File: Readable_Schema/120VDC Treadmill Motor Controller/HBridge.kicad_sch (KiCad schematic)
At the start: 56 parts, among them J2 OSTT7020150, Q1 IPP60R060P7XKSA1, Q2 IPP60R060P7XKSA1, Q3 IPP60R060P7XKSA1, Q4 IPP60R060P7XKSA1, U1 UCC21530DWKR, U2 UCC21530DWKR

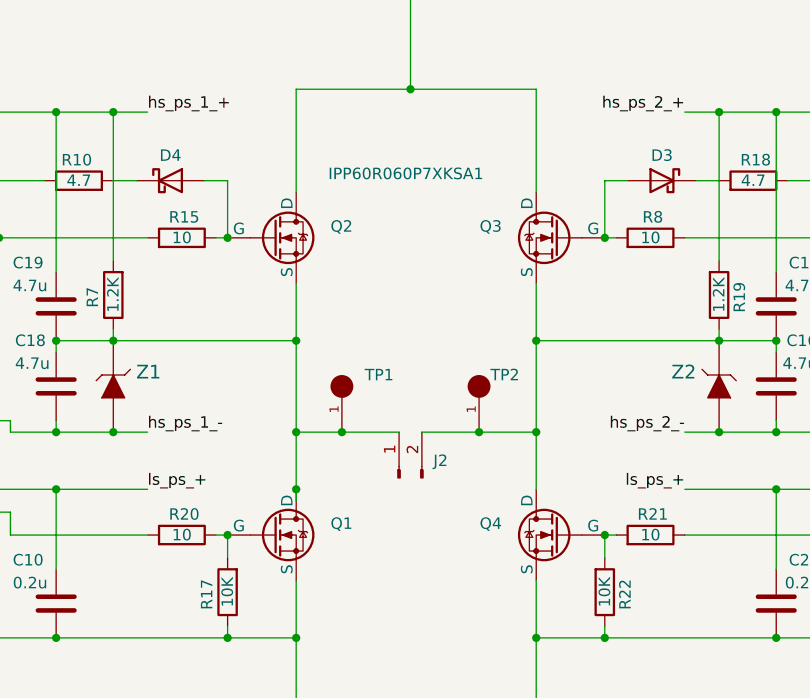
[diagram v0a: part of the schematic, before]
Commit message: -Updated kicad fet symbol to swap gate and drain numbers to match the datasheet
-There are not vertically mounted rectifier alternatives that are capable of 50 amps so stuck with the current one
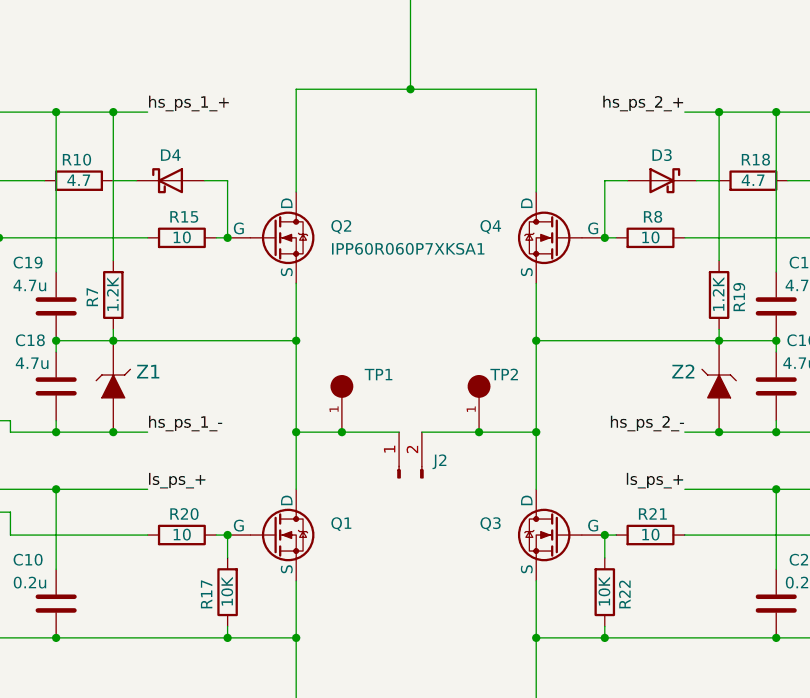
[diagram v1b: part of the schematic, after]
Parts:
- removed Q1, Q2, Q3, Q4: IPP60R060P7XKSA1, Package_TO_SOT_THT:TO-220-3_Vertical, symbol Simulation_SPICE:NMOS
- added Q1, Q2, Q3, Q4: IPP60R060P7XKSA1, Package_TO_SOT_THT:TO-220-3_Vertical, symbol Treadmill_Comp:IPP60R060P7XKSA1
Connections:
- net 170V Rect: now also Q2.2 (D), Q4.2 (D)
- net i_sense_+: now also Q1.3 (S), Q3.3 (S)
- net at D3.2 (A), R8.2: now also Q4.1 (G)
- net at C15.2, C16.1, J2.2 (Pin_2)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: now also Q3.2 (D), Q4.3 (S)
- net at C18.1, C19.2, J2.1 (Pin_1)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: now also Q1.2 (D), Q2.3 (S)
- net at D4.2 (A), R15.1: now also Q2.1 (G)
- net at R17.2, R20.1: now also Q1.1 (G)
- net at R21.2, R22.2: now also Q3.1 (G)

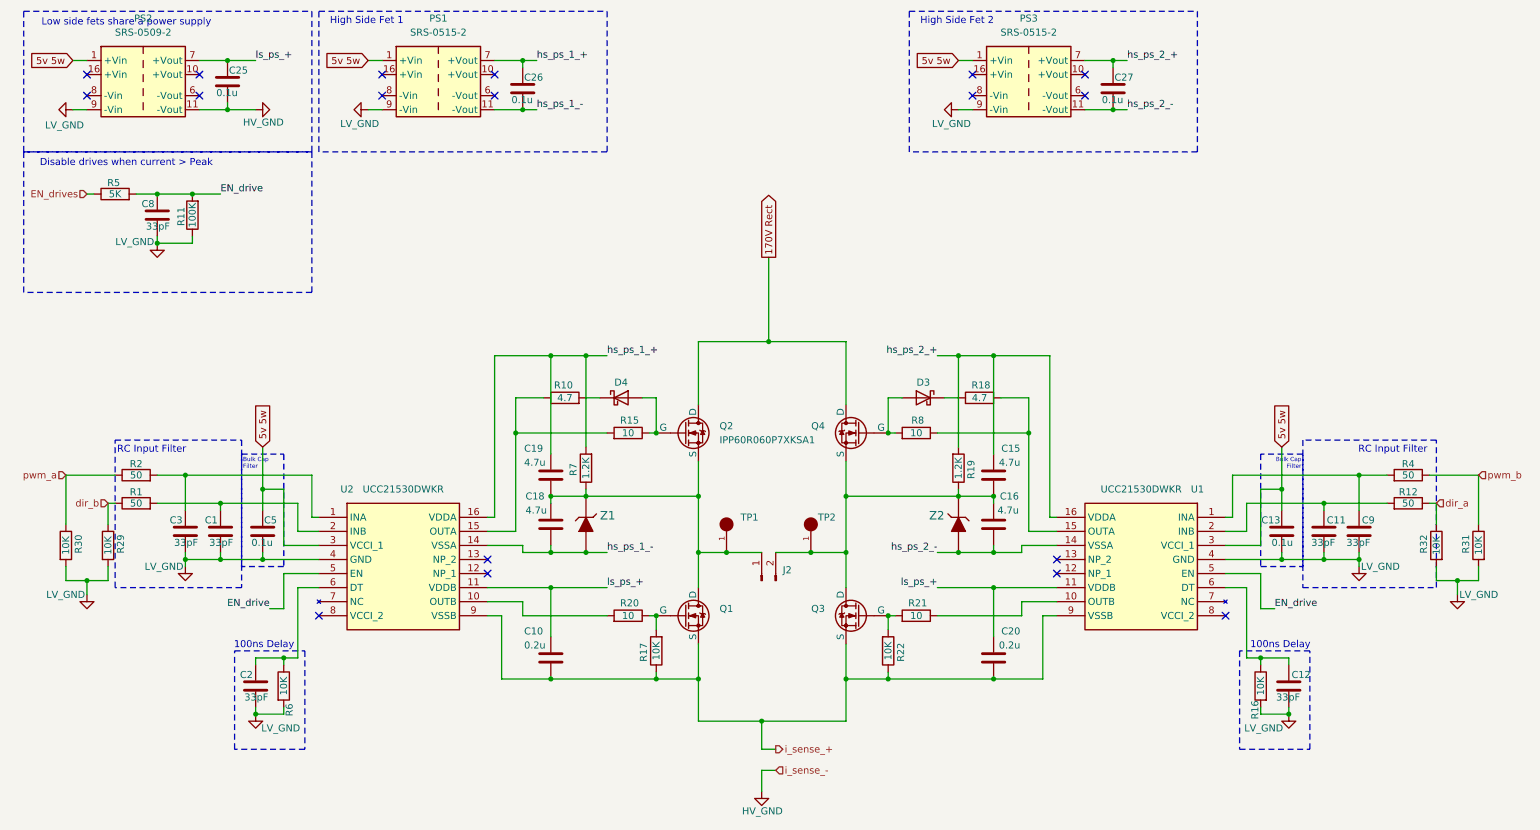
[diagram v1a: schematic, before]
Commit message: -Feedback Schema --fixed some of fine details surrounding pulling some stuff to ground --missing bypass caps --resizing footprints
-H bridge
--Chose higher current rating schottky diode
--Resized footprints and chose better
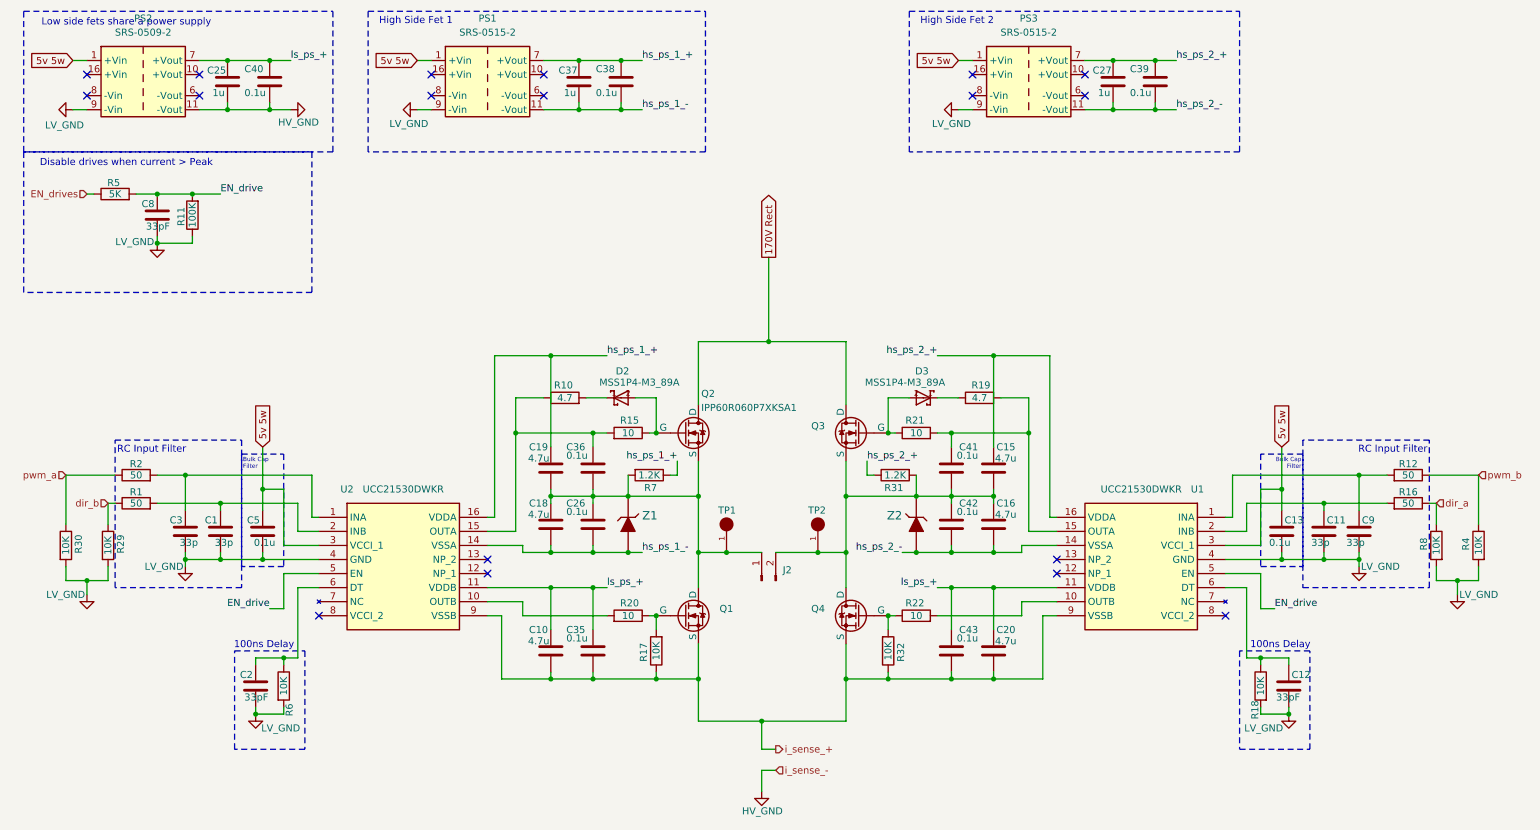
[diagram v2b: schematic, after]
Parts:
- removed D3, D4: NSR0340HT1G, Diode_SMD:D_SOD-323, symbol Diode:NSR0340HT1G
- added C35, C36, C38, C39, C40, C41, C42, C43: 0.1u, Capacitor_SMD:C_0201_0603Metric_Pad0.64x0.40mm_HandSolder, symbol Device:C
- added C37: 1u, Capacitor_SMD:C_0402_1005Metric_Pad0.74x0.62mm_HandSolder, symbol Device:C
- added D2, D3: MSS1P4-M3_89A, MSS1P4-M3_89A:DIODE_MSS1P4-M3_89A, symbol Treadmill_Comp:MSS1P4-M3_89A
- C1, C11, C3, C9: value 33pF -> 33p
- C10, C20: value 0.2u -> 4.7u; footprint Capacitor_SMD:C_0402_1005Metric_Pad0.74x0.62mm_HandSolder -> Capacitor_SMD:C_0201_0603Metric_Pad0.64x0.40mm_HandSolder
- C13, C15, C16, C18, C19, C26, C5: footprint Capacitor_SMD:C_0402_1005Metric_Pad0.74x0.62mm_HandSolder -> Capacitor_SMD:C_0201_0603Metric_Pad0.64x0.40mm_HandSolder
- C25, C27: value 0.1u -> 1u
- R10: footprint Resistor_SMD:R_0201_0603Metric_Pad0.64x0.40mm_HandSolder -> Resistor_SMD:R_1206_3216Metric_Pad1.30x1.75mm_HandSolder
- R16: value 10K -> 50
- R18: value 4.7 -> 10K
- R19: value 1.2K -> 4.7; footprint Resistor_SMD:R_0201_0603Metric_Pad0.64x0.40mm_HandSolder -> Resistor_SMD:R_1206_3216Metric_Pad1.30x1.75mm_HandSolder
- R22: value 10K -> 10; footprint Resistor_SMD:R_0201_0603Metric_Pad0.64x0.40mm_HandSolder -> Resistor_SMD:R_1206_3216Metric_Pad1.30x1.75mm_HandSolder
- R31: value 10K -> 1.2K
- R4: value 50 -> 10K
- R8: value 10 -> 10K; footprint Resistor_SMD:R_1206_3216Metric_Pad1.30x1.75mm_HandSolder -> Resistor_SMD:R_0201_0603Metric_Pad0.64x0.40mm_HandSolder
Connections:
- net 170V Rect: now also Q3.2 (D); no longer Q4.2 (D)
- net HV_GND: now also C40.2
- net LV_GND: now also R18.2, R4.2, R8.2; no longer R16.2, R31.2, R32.2
- net dir_a: now also R16.1, R8.1; no longer R12.1, R32.1
- net hs_ps_1_+: now also R7.1, C37.1, C38.1; no longer C26.1, R7.2
- net hs_ps_1_-: now also C37.2, C38.2
- net hs_ps_2_+: now also R31.1, C39.1; no longer R19.2
- net hs_ps_2_-: now also C39.2, C42.2
- net i_sense_+: now also Q4.3 (S), R32.1, C35.2, C43.2; no longer Q3.3 (S), R22.1
- net ls_ps_+: now also C35.1, C40.1, C43.1
- net pwm_b: now also R12.1; no longer R31.1
- net at C9.1, U1.1 (INA): now also R12.2; no longer R4.2
- net at U1.10 (OUTB): now also R22.2; no longer R21.1
- net at C11.1, U1.2 (INB): now also R16.2; no longer R12.2
- net at C12.1, U1.6 (DT): now also R18.1; no longer R16.1
- net at C15.2, C16.1, J2.2 (Pin_2)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: now also Q3.3 (S), Q4.2 (D), R31.2, C41.2, C42.1; no longer Q3.2 (D), Q4.3 (S), R19.1
- net at C18.1, C19.2, J2.1 (Pin_1)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: now also C26.1, R7.2, C36.2; no longer R7.1
- net at R10.2: now also D2.1
- net at Q2.1 (G), R15.1: now also D2.2
- net at Q4.1 (G): now also R22.1, R32.2; no longer R8.2
- net at R10.1, R15.2, U2.15 (OUTA): now also C36.1
- new net: C41.1, R19.1, R21.2, U1.15 (OUTA)
- new net: D3.2, Q3.1 (G), R21.1
- new net: D3.1, R19.2
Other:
- moved on the sheet: C26, PS1, R7, TP2, Z1

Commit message: -Changed to a 15w 5v power supply instead of a 5w. (Achieved nothing else wtf)
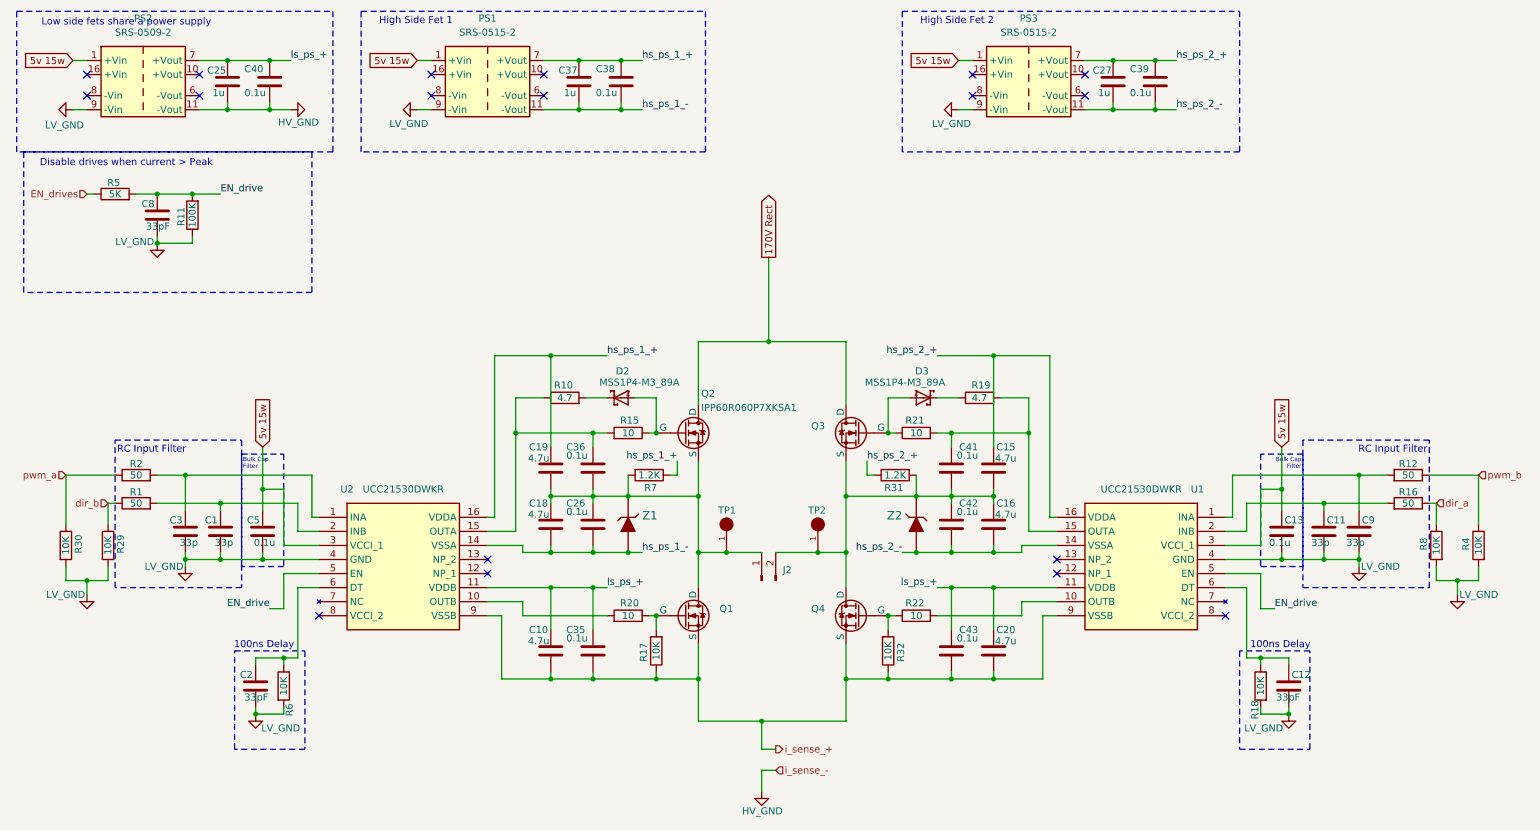
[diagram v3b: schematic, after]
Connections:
- net 5v 5w renamed 5v 15w
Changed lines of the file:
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@@
 	(paper "A4")
 	(rectangle
-		(start 74.93 12.7)
+		(start 73.66 12.7)
 		(end 135.89 38.1)
 		(stroke
@@
 	)
 	(rectangle
-		(start 172.72 12.7)
+		(start 171.45 12.7)
 		(end 232.41 38.1)
 		(stroke
@@
 	)
 	(rectangle
-		(start 12.7 12.7)
+		(start 11.43 12.7)
 		(end 68.58 38.1)
 		(stroke
@@
 		)
 	)
-	(global_label "5v 5w"
+	(global_label "5v 15w"
 		(shape input)
 		(at 21.59 21.59 180)
@@
 		)
 		(property "Intersheetrefs" "${INTERSHEET_REFS}"
-			(at 12.9201 21.59 0)
+			(at 11.7106 21.59 0)
 			(effects
 				(font
@@
 		)
 	)
-	(global_label "5v 5w"
+	(global_label "5v 15w"
 		(shape input)
 		(at 181.61 21.59 180)
@@
 		)
 		(property "Intersheetrefs" "${INTERSHEET_REFS}"
-			(at 172.9401 21.59 0)
+			(at 171.7306 21.59 0)
 			(effects
 				(font
@@
 		)
 	)
-	(global_label "5v 5w"
+	(global_label "5v 15w"
 		(shape input)
 		(at 55.88 91.44 90)
@@
 		)
 		(property "Intersheetrefs" "${INTERSHEET_REFS}"
-			(at 55.88 82.7701 90)
+			(at 55.88 81.5606 90)
 			(effects
 				(font
@@
 		)
 	)
-	(global_label "5v 5w"
+	(global_label "5v 15w"
 		(shape input)
 		(at 240.03 91.44 90)
@@
 		)
 		(property "Intersheetrefs" "${INTERSHEET_REFS}"
-			(at 240.03 82.7701 90)
+			(at 240.03 81.5606 90)
 			(effects
 				(font
@@
 		)
 	)
-	(global_label "5v 5w"
+	(global_label "5v 15w"
 		(shape input)
 		(at 83.82 21.59 180)
@@
 		)
 		(property "Intersheetrefs" "${INTERSHEET_REFS}"
-			(at 75.1501 21.59 0)
+			(at 73.9406 21.59 0)
 			(effects
 				(font

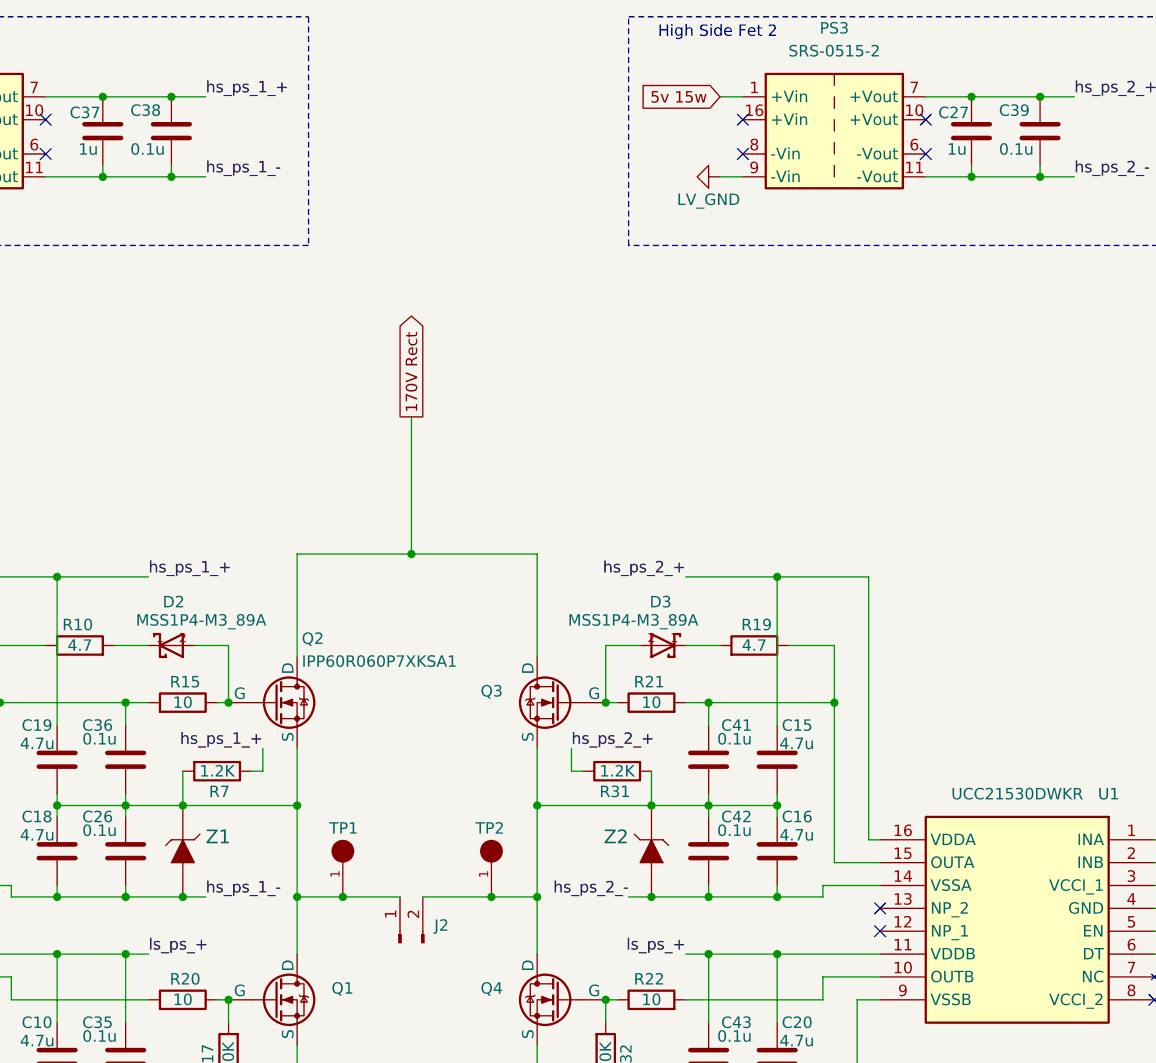
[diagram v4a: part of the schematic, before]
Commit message: -Think we're finished with the schematic (finally) --Upped the LED resistors and added a few more supporting caps for the 3.3v iso supply in the feedback schema
-Started placing footprints
--Now that we're using how air instead of oven I'm not going to try and keep all SMD components on the same side anymore
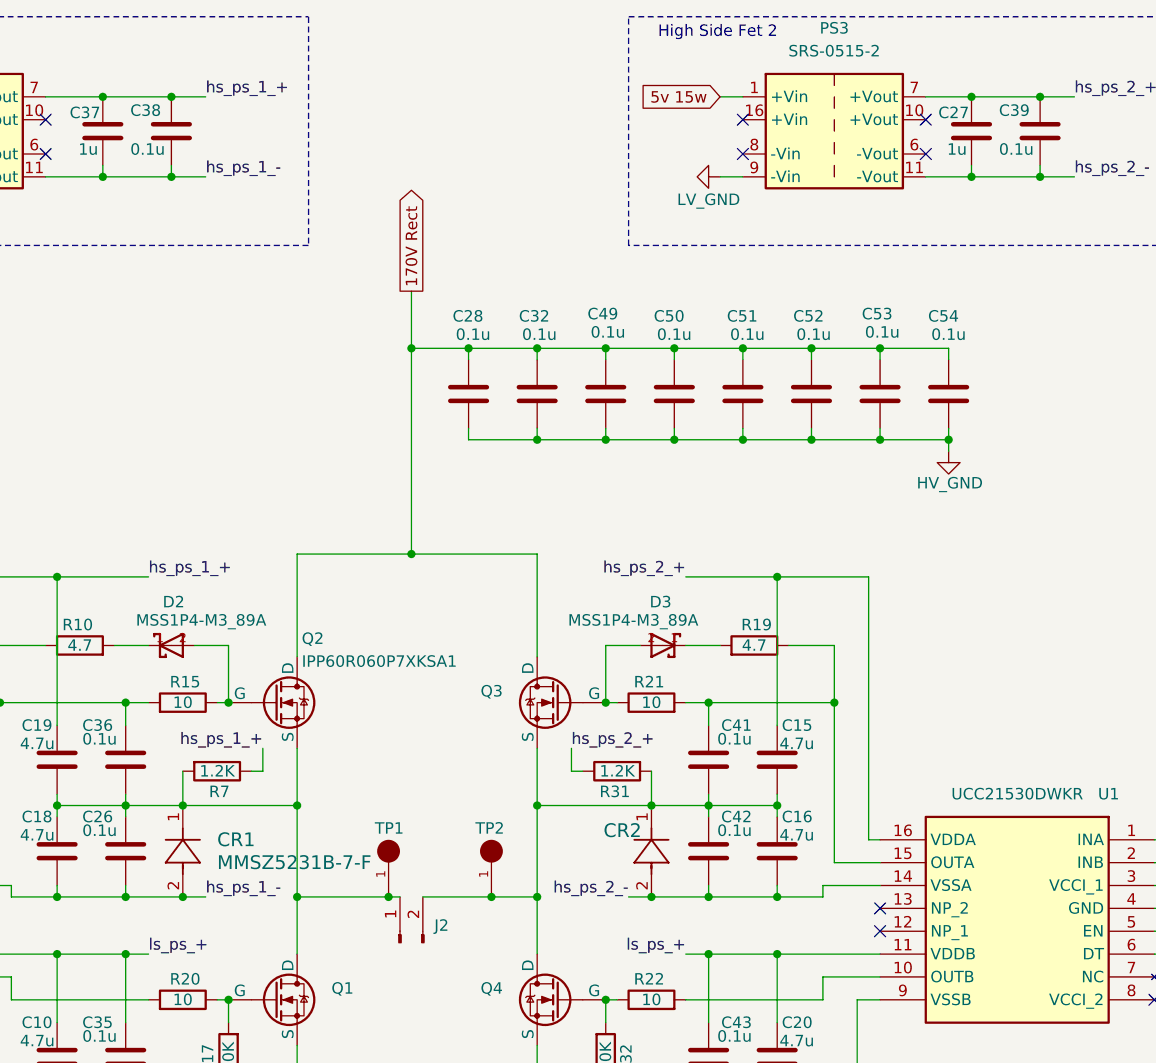
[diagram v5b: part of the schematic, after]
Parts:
- removed Z1, Z2: MMSZ5231B-7-F, Treadmill_Feet:SOD123_DIO, symbol dk_Diodes-Zener-Single:MMSZ5231B-7-F
- added C28, C32, C49, C50, C51, C52, C53, C54: C3216X7T2V104M160AA, Capacitor_SMD:C_1206_3216Metric_Pad1.33x1.80mm_HandSolder, symbol Device:C
- added CR1, CR2: MMSZ5231B-7-F, Treadmill_Feet:SOD123_DIO, symbol Treadmill_Comp:MMSZ5231B-7-F
- D2, D3: footprint MSS1P4-M3_89A:DIODE_MSS1P4-M3_89A -> Treadmill_Feet:DIODE_MSS1P4-M3_89A
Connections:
- net 170V Rect: now also C28.1, C32.1, C49.1, C50.1, C51.1, C52.1, C53.1, C54.1
- net HV_GND: now also C28.2, C32.2, C49.2, C50.2, C51.2, C52.2, C53.2, C54.2
- net hs_ps_1_-: now also CR1.2
- net hs_ps_2_-: now also CR2.2
- net at C15.2, C16.1, C41.2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: now also CR2.1
- net at C18.1, C19.2, C26.1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: now also CR1.1
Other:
- moved on the sheet: TP1

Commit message: -Getting fairly stuck on the best way to layout some of these high voltage components, especially the high current line that requires a pour rather than a trace
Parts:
- added NT1, NT2, NT3, NT4: NetTie_2, NetTie:NetTie-2_THT_Pad0.3mm, symbol Device:NetTie_2
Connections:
- net i_sense_+: now also NT3.1, NT4.2; no longer C10.2, C20.2, C35.2, C43.2, R17.1, R32.1, U1.9 (VSSB), U2.9 (VSSB)
- net at C15.2, C16.1, C41.2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: now also NT2.2; no longer J2.2 (Pin_2), Q3.3 (S), Q4.2 (D), TP2.1
- net at C18.1, C19.2, C26.1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: now also NT1.1; no longer J2.1 (Pin_1), Q1.2 (D), Q2.3 (S), TP1.1
- new net: C20.2, C43.2, NT3.2, R32.1, U1.9 (VSSB)
- new net: C10.2, C35.2, NT4.1, R17.1, U2.9 (VSSB)
- new net: J2.2 (Pin_2), NT2.1, Q3.3 (S), Q4.2 (D), TP2.1
- new net: J2.1 (Pin_1), NT1.2, Q1.2 (D), Q2.3 (S), TP1.1
